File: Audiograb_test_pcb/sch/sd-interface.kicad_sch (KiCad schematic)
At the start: 35 parts, among them J15 F32Q-1A7H1-11022, J16 MEM2075-00-140-01-A, J17 5V_out, J19 3V3_in, Q1 Q_PMOS_GSD, T12 TestPoint, T13 TestPoint, T14 TestPoint, T15 TestPoint, T16 TestPoint, T17 TestPoint, T18 Select, T19 Enable, T20 TestPoint, T21 TestPoint, T22 TestPoint, T23 TestPoint, T24 TestPoint, T25 TestPoint, U10 CD4043BDR, U11 TPS22919DCKR, U8 MAX4996LETG_

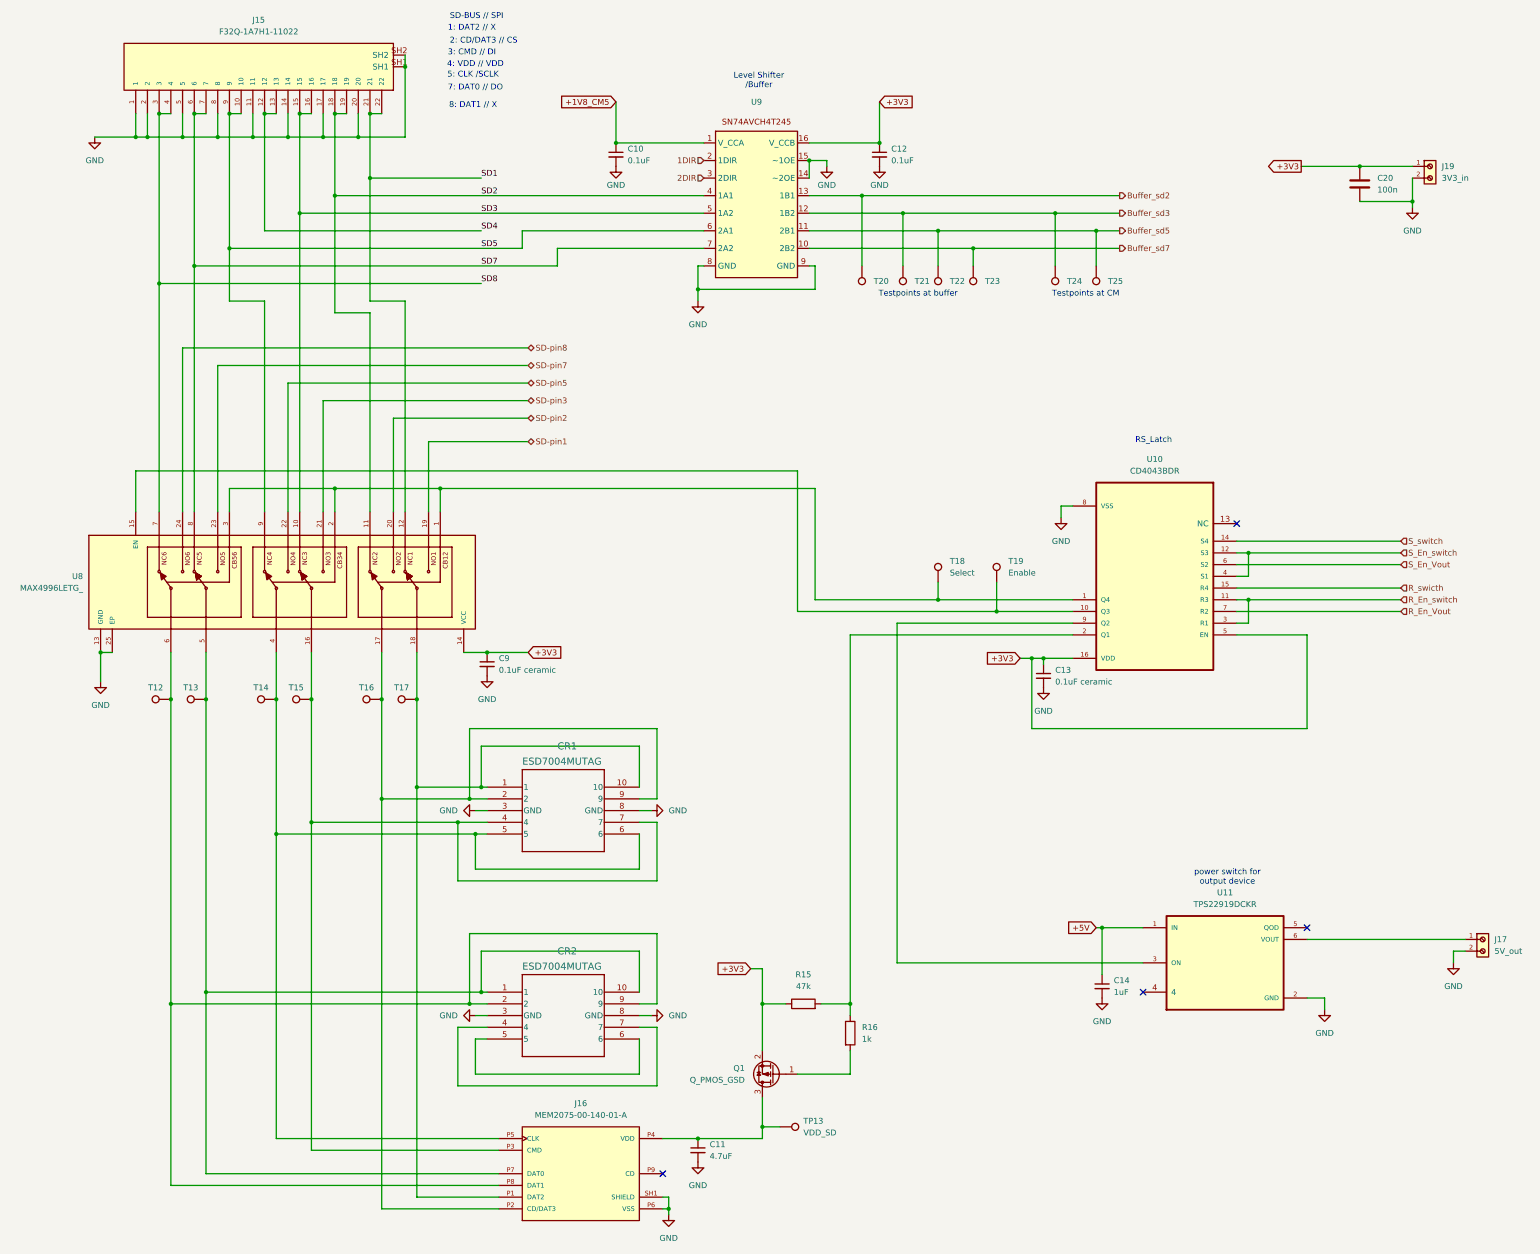
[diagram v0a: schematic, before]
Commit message: La til hard shutdown for modem, la til signal SAFE_PWR_REMOVE, fikset nummerering testpoints ++ noen småting
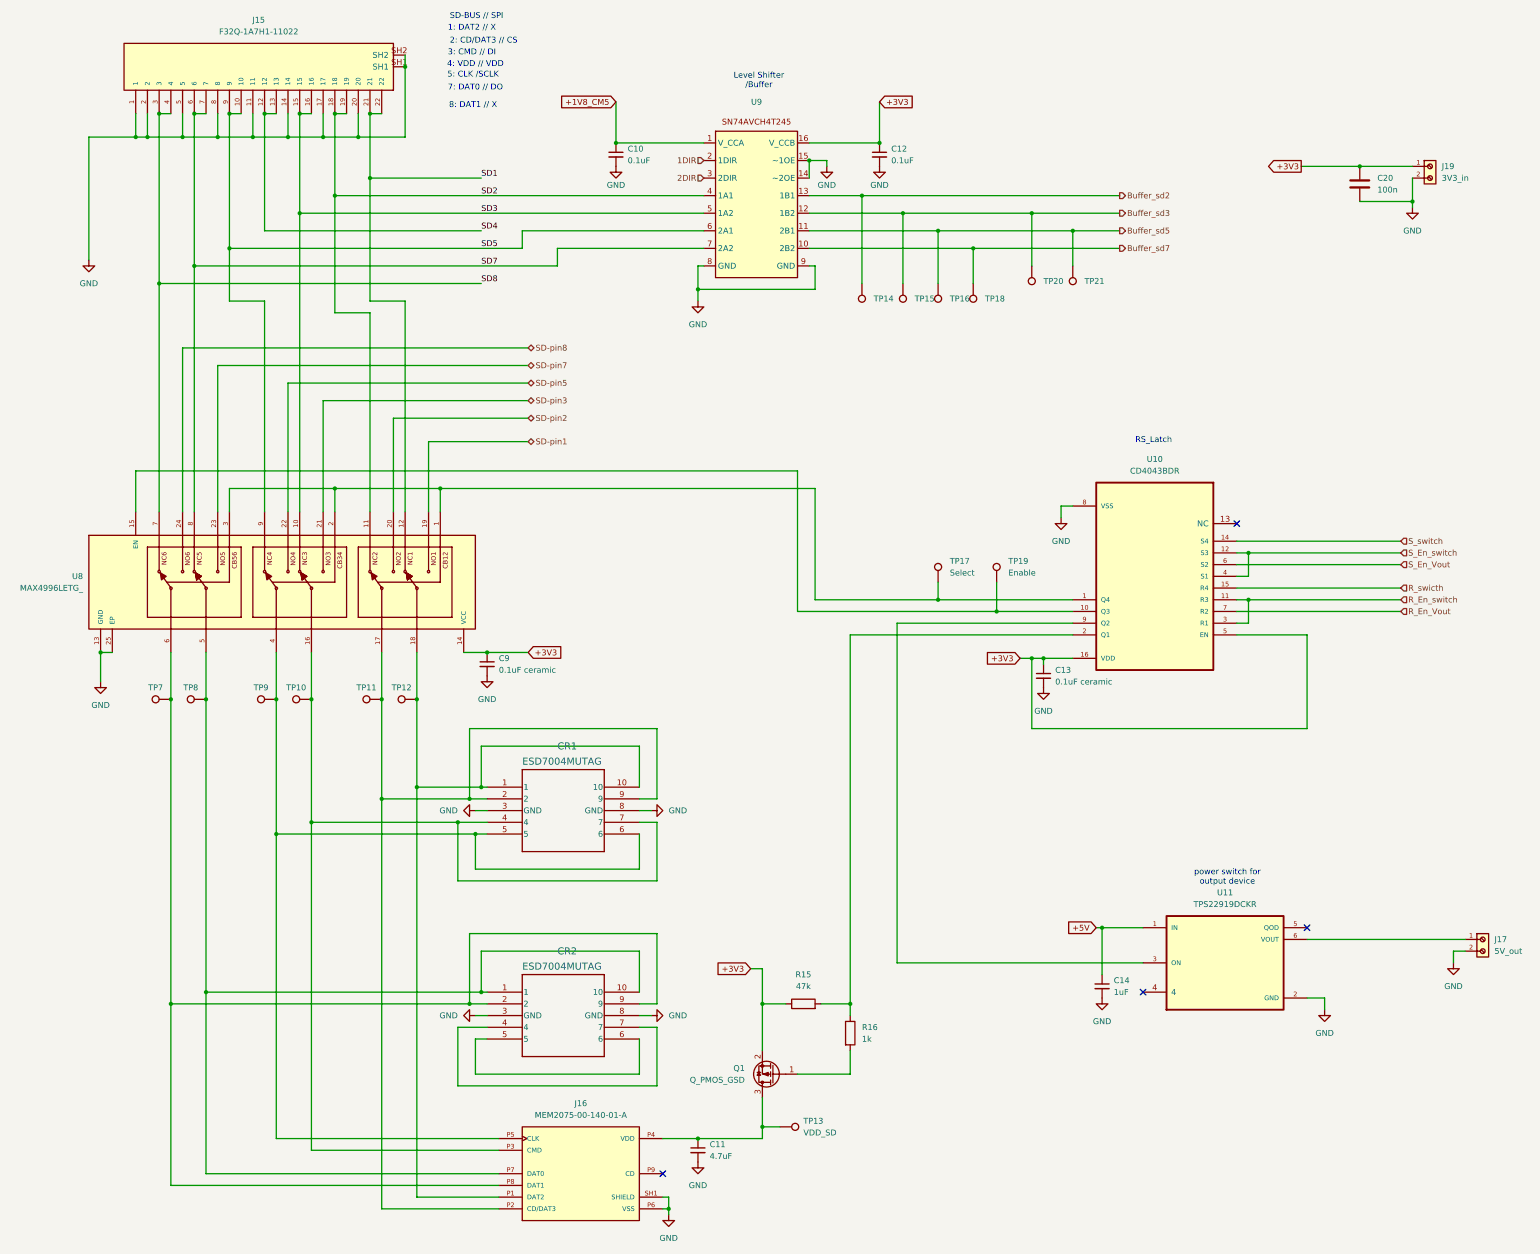
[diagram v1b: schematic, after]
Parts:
- CR1, CR2: footprint ESD7004MUTAG:UDFN10_517BB_ONS -> UDFN10_517BB_ONS
- renumbered T15 to TP10, T16 to TP11, T17 to TP12, T20 to TP14, T21 to TP15, T22 to TP16, T18 to TP17, T23 to TP18, T19 to TP19, T24 to TP20, T25 to TP21, T12 to TP7, T13 to TP8, T14 to TP9
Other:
- note removed: "Testpoints at CM"
- note removed: "Testpoints at buffer"
- moved on the sheet: TP14, TP15, TP16, TP18, TP20, TP21
